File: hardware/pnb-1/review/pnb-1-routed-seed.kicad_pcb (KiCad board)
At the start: 2 copper layers, 58 x 42 mm, 37 parts, among them J1 USB-C 16P, J3 DTR 2x6 DNP, J4 UART 1x4, SW1 BOOT, SW2 RESET, U1 ESP32-S3-MINI-1-N8, U2 AMS1117-3.3, U3 SCD41-D-R2, U4 BH1750FVI-TR

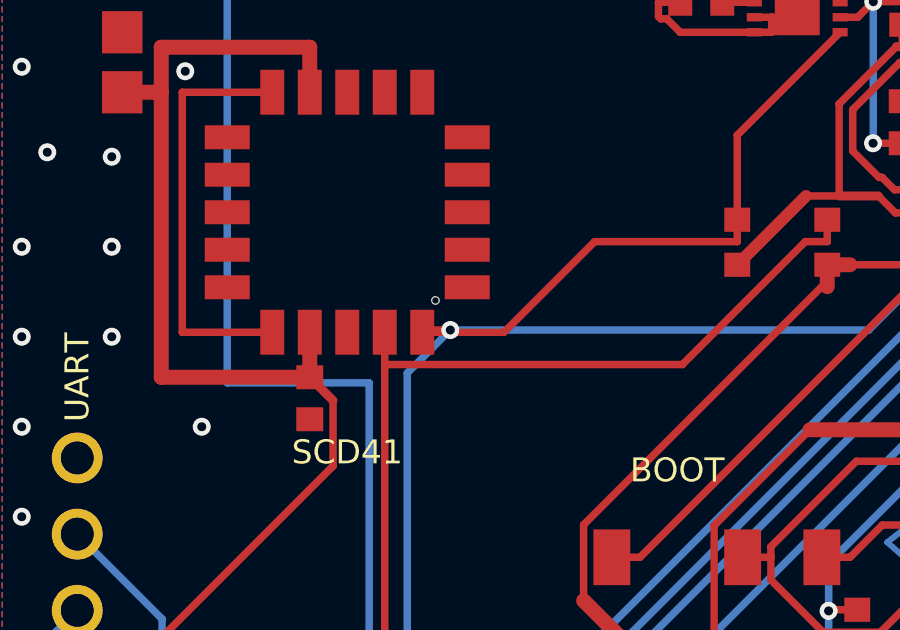
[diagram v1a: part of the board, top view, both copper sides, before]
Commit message: docs(pcb): record fabrication review evidence
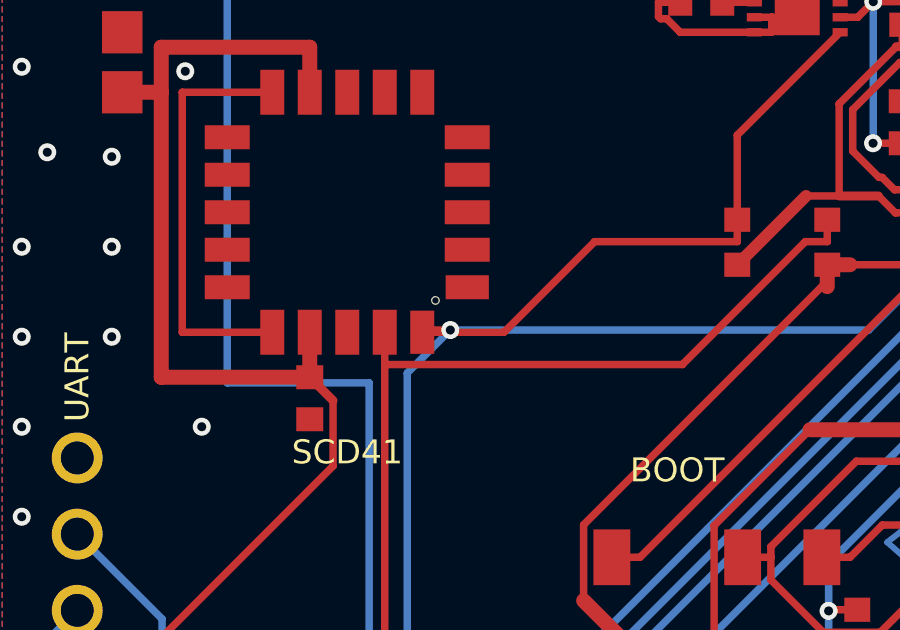
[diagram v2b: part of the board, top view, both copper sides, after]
